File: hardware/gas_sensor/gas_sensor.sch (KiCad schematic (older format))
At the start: 10 parts, among them J1 Conn_01x04, U1 LM393

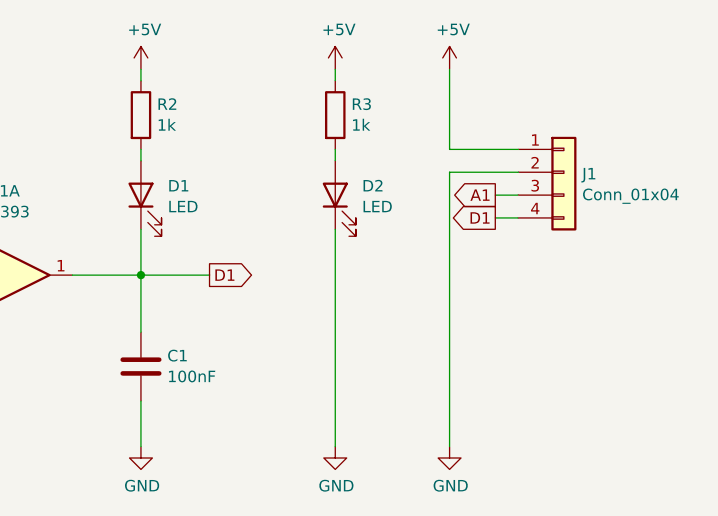
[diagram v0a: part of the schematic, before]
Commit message: update gas sensor
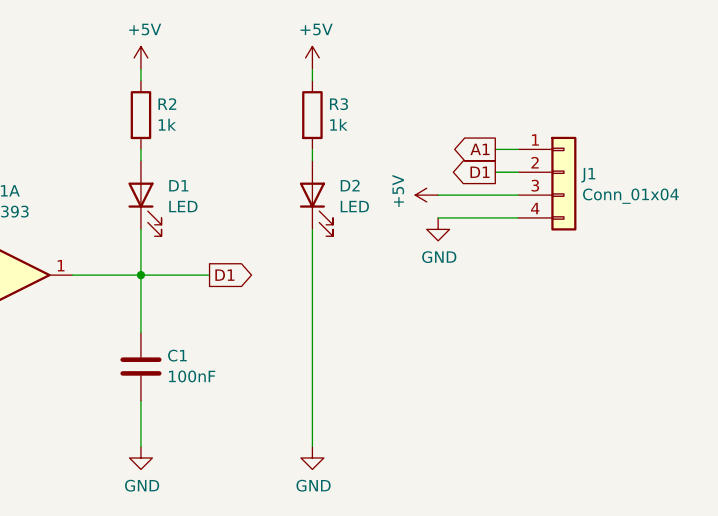
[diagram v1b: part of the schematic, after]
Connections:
- net +5V: now also J1.3 (Pin_3); no longer J1.1 (Pin_1)
- net A1: now also J1.1 (Pin_1); no longer J1.3 (Pin_3)
- net D1: now also J1.2 (Pin_2); no longer J1.4 (Pin_4)
- net GND: now also J1.4 (Pin_4); no longer J1.2 (Pin_2)
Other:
- moved on the sheet: D2, R3
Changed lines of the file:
@@
 EESchema Schematic File Version 4
-LIBS:gas_sensor-cache
 EELAYER 30 0
 EELAYER END
@@
 Text GLabel 2900 1450 2    50   Output ~ 0
 A1
-Text GLabel 7100 1700 0    50   Output ~ 0
+Text GLabel 7100 1500 0    50   Output ~ 0
 A1
-Text GLabel 7100 1800 0    50   Output ~ 0
+Text GLabel 7100 1600 0    50   Output ~ 0
 D1
 Wire Wire Line
@@
 L power:+5V #PWR0110
 U 1 1 5F35CEC0
-P 6400 1150
-F 0 "#PWR0110" H 6400 1000 50  0001 C CNN
-F 1 "+5V" H 6415 1323 50  0000 C CNN
-F 2 "" H 6400 1150 50  0001 C CNN
-F 3 "" H 6400 1150 50  0001 C CNN
-	1    6400 1150
+P 6300 1150
+F 0 "#PWR0110" H 6300 1000 50  0001 C CNN
+F 1 "+5V" H 6315 1323 50  0000 C CNN
+F 2 "" H 6300 1150 50  0001 C CNN
+F 3 "" H 6300 1150 50  0001 C CNN
+	1    6300 1150
 	1    0    0    -1
 $EndComp
@@
 L Device:R R3
 U 1 1 5F35CEC6
-P 6400 1350
-F 0 "R3" H 6470 1396 50  0000 L CNN
-F 1 "1k" H 6470 1305 50  0000 L CNN
-F 2 "Resistor_THT:R_Box_L13.0mm_W4.0mm_P9.00mm" V 6330 1350 50  0001 C CNN
-F 3 "~" H 6400 1350 50  0001 C CNN
-	1    6400 1350
-	1    0    0    -1
-$EndComp
-Wire Wire Line
-	6400 1150 6400 1200
+P 6300 1350
+F 0 "R3" H 6370 1396 50  0000 L CNN
+F 1 "1k" H 6370 1305 50  0000 L CNN
+F 2 "Resistor_THT:R_Box_L13.0mm_W4.0mm_P9.00mm" V 6230 1350 50  0001 C CNN
+F 3 "~" H 6300 1350 50  0001 C CNN
+	1    6300 1350
+	1    0    0    -1
+$EndComp
+Wire Wire Line
+	6300 1150 6300 1200
 $Comp
 L Device:LED D2
 U 1 1 5F35CECD
-P 6400 1700
-F 0 "D2" V 6439 1583 50  0000 R CNN
-F 1 "LED" V 6348 1583 50  0000 R CNN
-F 2 "LED_THT:LED_D3.0mm" H 6400 1700 50  0001 C CNN
-F 3 "~" H 6400 1700 50  0001 C CNN
-	1    6400 1700
+P 6300 1700
+F 0 "D2" V 6339 1583 50  0000 R CNN
+F 1 "LED" V 6248 1583 50  0000 R CNN
+F 2 "LED_THT:LED_D3.0mm" H 6300 1700 50  0001 C CNN
+F 3 "~" H 6300 1700 50  0001 C CNN
+	1    6300 1700
 	0    -1   -1   0
 $EndComp
 Wire Wire Line
-	6400 1550 6400 1500
+	6300 1550 6300 1500
 Wire Wire Line
 	5550 1850 5550 2050
@@
 L power:GND #PWR0111
 U 1 1 5F35D33B
-P 6400 2800
-F 0 "#PWR0111" H 6400 2550 50  0001 C CNN
-F 1 "GND" H 6405 2627 50  0000 C CNN
-F 2 "" H 6400 2800 50  0001 C CNN
-F 3 "" H 6400 2800 50  0001 C CNN
-	1    6400 2800
-	1    0    0    -1
-$EndComp
-Wire Wire Line
-	6400 1850 6400 2800
+P 6300 2800
+F 0 "#PWR0111" H 6300 2550 50  0001 C CNN
+F 1 "GND" H 6305 2627 50  0000 C CNN
+F 2 "" H 6300 2800 50  0001 C CNN
+F 3 "" H 6300 2800 50  0001 C CNN
+	1    6300 2800
+	1    0    0    -1
+$EndComp
+Wire Wire Line
+	6300 1850 6300 2800
 $Comp
 L power:+5V #PWR0112
 U 1 1 5F3634EE
-P 6900 1150
-F 0 "#PWR0112" H 6900 1000 50  0001 C CNN
-F 1 "+5V" H 6915 1323 50  0000 C CNN
-F 2 "" H 6900 1150 50  0001 C CNN
-F 3 "" H 6900 1150 50  0001 C CNN
-	1    6900 1150
-	1    0    0    -1
-$EndComp
-Wire Wire Line
-	7200 1700 7100 1700
-Wire Wire Line
-	7200 1800 7100 1800
+P 6850 1700
+F 0 "#PWR0112" H 6850 1550 50  0001 C CNN
+F 1 "+5V" H 6865 1873 50  0000 C CNN
+F 2 "" H 6850 1700 50  0001 C CNN
+F 3 "" H 6850 1700 50  0001 C CNN
+	1    6850 1700
+	0    -1   -1   0
+$EndComp
 $Comp
 L power:GND #PWR0113
 U 1 1 5F365C4A
-P 6900 2800
-F 0 "#PWR0113" H 6900 2550 50  0001 C CNN
-F 1 "GND" H 6905 2627 50  0000 C CNN
-F 2 "" H 6900 2800 50  0001 C CNN
-F 3 "" H 6900 2800 50  0001 C CNN
-	1    6900 2800
-	1    0    0    -1
-$EndComp
-Wire Wire Line
-	6900 1600 6900 2800
-Wire Wire Line
-	6900 1600 7200 1600
-Wire Wire Line
-	6900 1500 6900 1150
-Wire Wire Line
-	6900 1500 7200 1500
+P 6850 1800
+F 0 "#PWR0113" H 6850 1550 50  0001 C CNN
+F 1 "GND" H 6855 1627 50  0000 C CNN
+F 2 "" H 6850 1800 50  0001 C CNN
+F 3 "" H 6850 1800 50  0001 C CNN
+	1    6850 1800
+	1    0    0    -1
+$EndComp
 Wire Wire Line
 	1100 1150 1100 2500
@@
 Wire Wire Line
 	1400 1950 1400 2800
+Wire Wire Line
+	7200 1500 7100 1500
+Wire Wire Line
+	7200 1600 7100 1600
+Wire Wire Line
+	6850 1700 7200 1700
+Wire Wire Line
+	6850 1800 7200 1800
 $EndSCHEMATC

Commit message: Update gas_sensor.sch
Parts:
- R2, R3: value 1k -> 220
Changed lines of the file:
@@
 P 5550 1350
 F 0 "R2" H 5620 1396 50  0000 L CNN
-F 1 "1k" H 5620 1305 50  0000 L CNN
+F 1 "220" H 5620 1305 50  0000 L CNN
 F 2 "Resistor_THT:R_Box_L13.0mm_W4.0mm_P9.00mm" V 5480 1350 50  0001 C CNN
 F 3 "~" H 5550 1350 50  0001 C CNN
@@
 P 6300 1350
 F 0 "R3" H 6370 1396 50  0000 L CNN
-F 1 "1k" H 6370 1305 50  0000 L CNN
+F 1 "220" H 6370 1305 50  0000 L CNN
 F 2 "Resistor_THT:R_Box_L13.0mm_W4.0mm_P9.00mm" V 6230 1350 50  0001 C CNN
 F 3 "~" H 6300 1350 50  0001 C CNN
